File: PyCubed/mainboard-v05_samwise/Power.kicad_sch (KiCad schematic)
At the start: 64 parts, among them J14 Conn_01x06, J19 Conn_01x06, Q2 MBT2222ADW1T1, Q3 MBT2222ADW1T1, U17 BQ25883RGER, U21 TPS7A4501DCQT, U4 ADM1176-1ARMZ-R7, U5 TPS54226PWPR, U6 LT3652HVIMSE#PBF

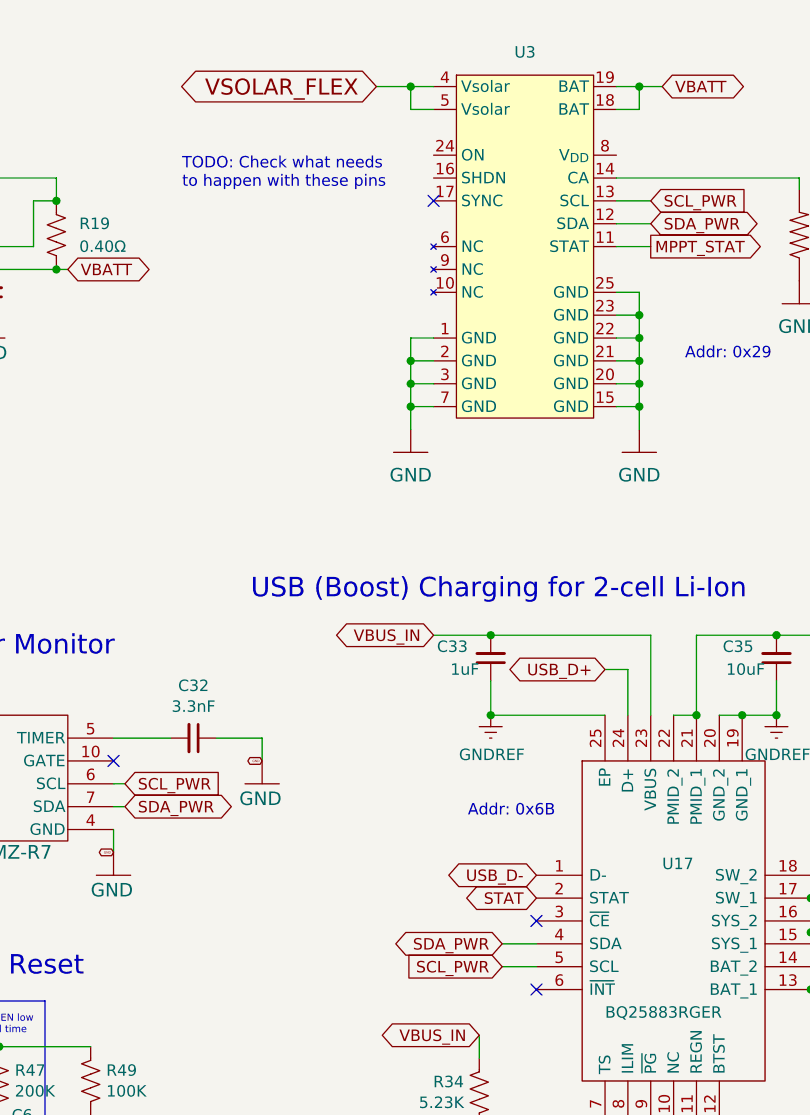
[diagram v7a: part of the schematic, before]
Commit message: changed usbc footprint
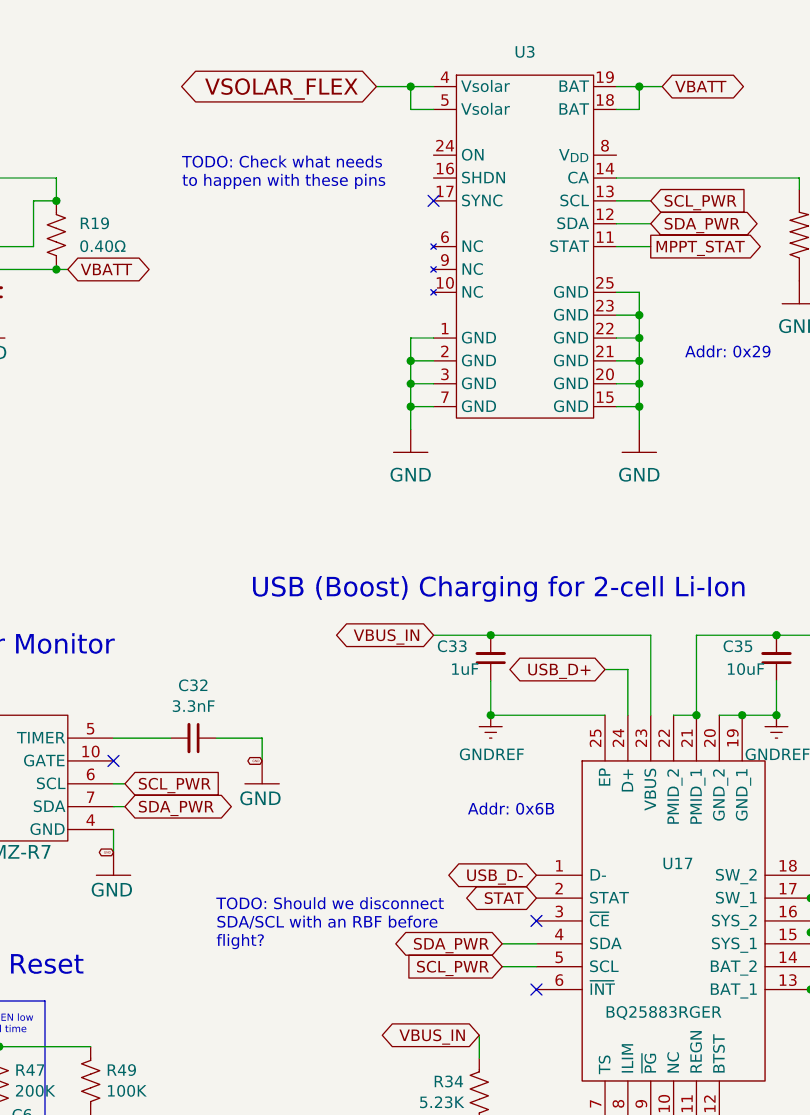
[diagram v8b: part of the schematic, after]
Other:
- note added: "TODO: Should we disconnect SDA/SCL with an RBF before flight?"
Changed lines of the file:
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@@
     (effects (font (size 0.889 0.889)) (justify right bottom))
+  )
+  (text "TODO: Should we disconnect \nSDA/SCL with an RBF before \nflight?"
+    (at 175.26 118.745 0)
+    (effects (font (size 1.27 1.27) (color 255 0 0 1)) (justify left bottom))
   )
   (text "Battery Power Monitor" (at 130.81 86.36 0)
